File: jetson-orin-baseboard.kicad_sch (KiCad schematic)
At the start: 4 parts

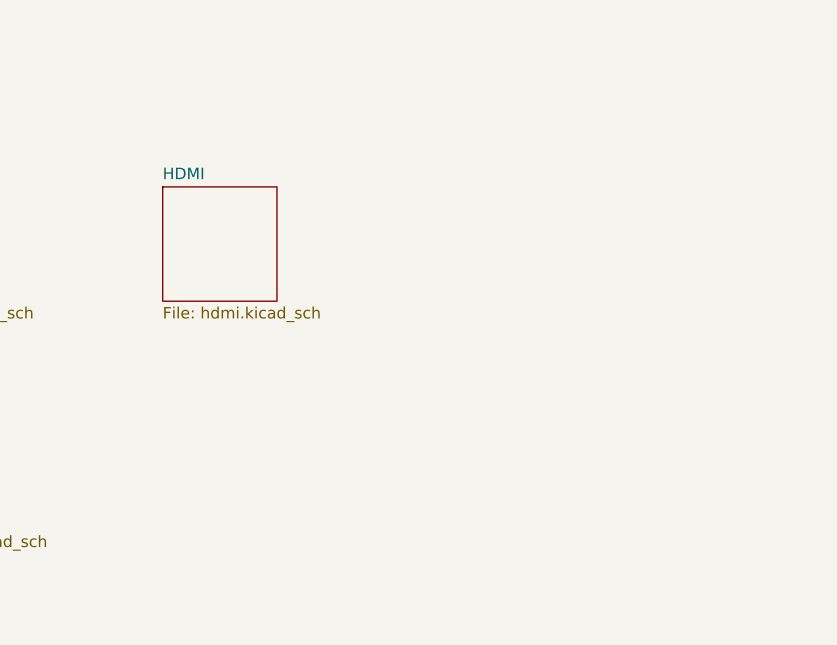
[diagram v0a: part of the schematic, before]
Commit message: 5/16 Commit: Sch Mods added and beginning Development on PCB layout
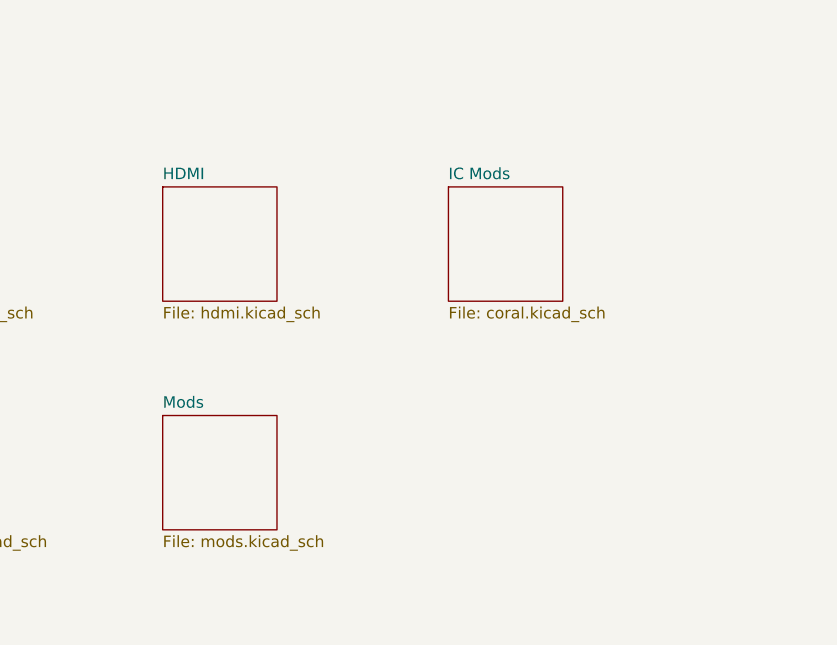
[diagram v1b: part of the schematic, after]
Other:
- added sheet IC Mods (coral.kicad_sch)
- added sheet Mods (mods.kicad_sch)
